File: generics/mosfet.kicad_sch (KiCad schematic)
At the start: 1 part, among them Q1 900mA

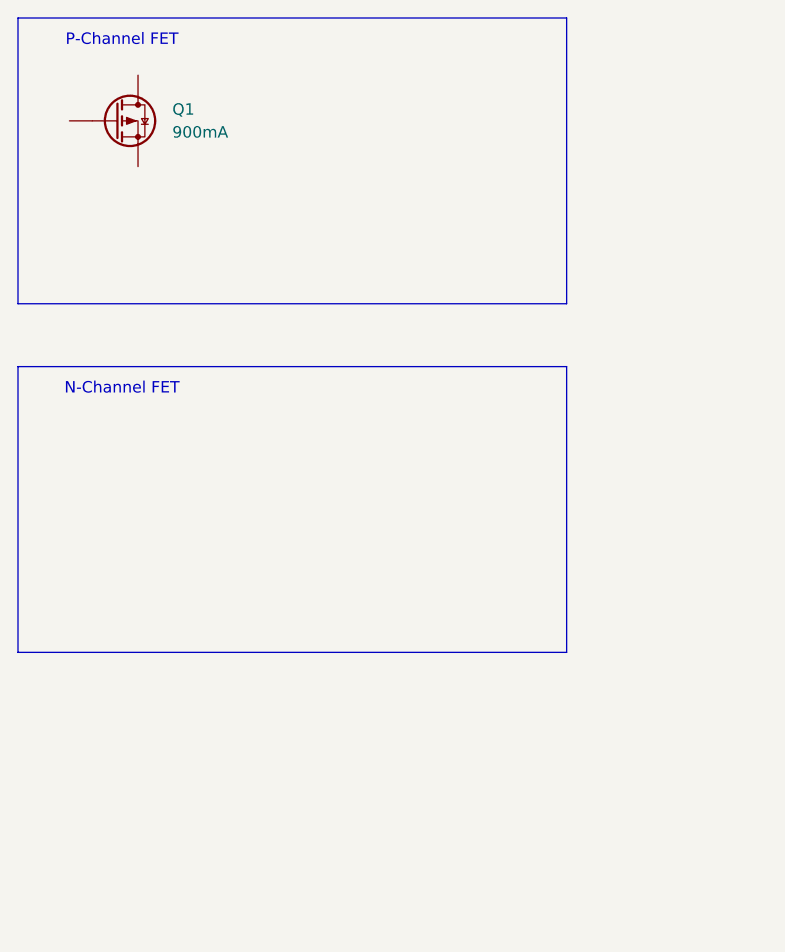
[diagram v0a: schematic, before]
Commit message: Add parts for V0 status indicator light project
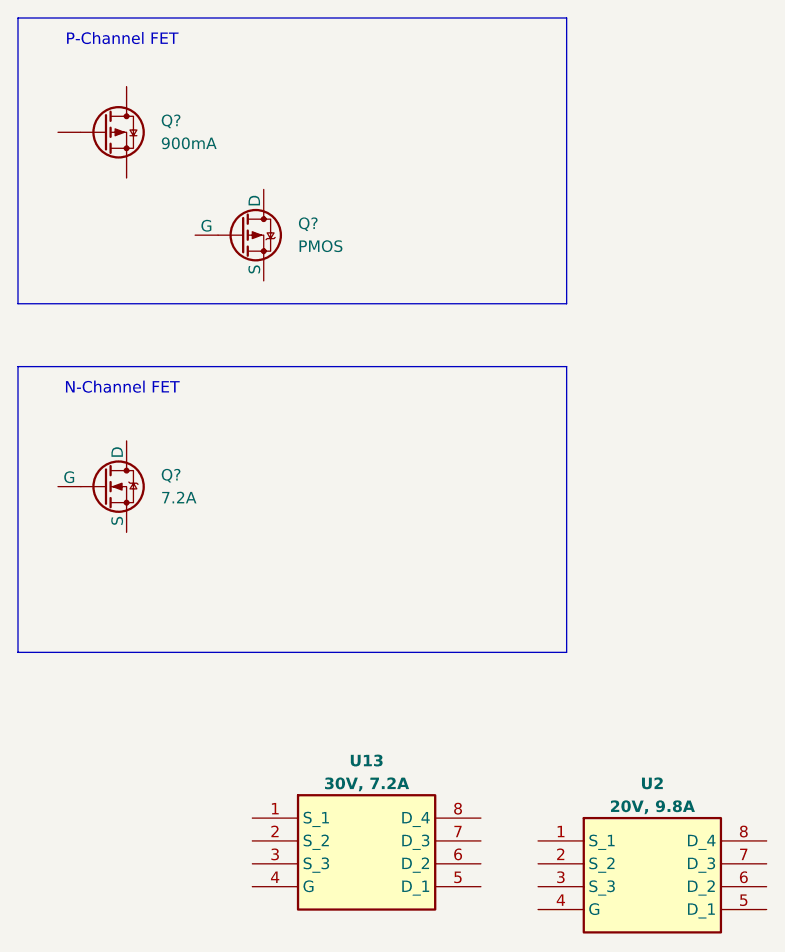
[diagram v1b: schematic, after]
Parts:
- added Q?: 7.2A, Package_SO:SO-8_3.9x4.9mm_P1.27mm, symbol Simulation_SPICE:NMOS
- added Q?: PMOS, symbol Simulation_SPICE:PMOS
- added U13: 30V, 7.2A, Package_SO:SO-8_3.9x4.9mm_P1.27mm, symbol Custom_Switch:DMN2028USS-13
- added U2: 20V, 9.8A, Custom_Switch:DMN2028USS-13, symbol Custom_Switch:DMN2028USS-13
- renumbered Q1 to Q?
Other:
- moved on the sheet: Q?
